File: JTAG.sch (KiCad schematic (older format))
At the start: 5 parts, among them J17 Conn_02x05_Odd_Even

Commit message: PVT
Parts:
- renumbered R89 to R79, R90 to R80, R91 to R81, RA10 to RA11
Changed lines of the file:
@@
 encoding utf-8
 Sheet 15 24
-Title "Phoenix DVT"
-Date "2020-05-18"
+Title "Phoenix PVT"
+Date "2020-07-19"
 Rev "1"
 Comp ""
@@
 P 7200 3700
 AR Path="/5E4B5786/5ED1E5C8" Ref="R?"  Part="1"
-AR Path="/5EF045E7/5ED1E5C8" Ref="R90"  Part="1"
-F 0 "R90" H 7258 3746 50  0000 L CNN
+AR Path="/5EF045E7/5ED1E5C8" Ref="R80"  Part="1"
+F 0 "R80" H 7258 3746 50  0000 L CNN
 F 1 "1k" H 7258 3655 50  0000 L CNN
 F 2 "Resistor-Chip:R_CHIP_1005_Hand_NoSilk" V 7250 3600 50  0001 C CNN
@@
 AR Path="/5E9E174E/5ED1E5DE" Ref="#PWR?"  Part="1"
 AR Path="/5E4B5786/5ED1E5DE" Ref="#PWR?"  Part="1"
-AR Path="/5EF045E7/5ED1E5DE" Ref="#PWR0287"  Part="1"
-F 0 "#PWR0287" H 5100 4450 50  0001 C CNN
+AR Path="/5EF045E7/5ED1E5DE" Ref="#PWR0275"  Part="1"
+F 0 "#PWR0275" H 5100 4450 50  0001 C CNN
 F 1 "GND" H 5100 4550 50  0000 C CNN
 F 2 "" H 5100 4700 50  0001 C CNN
@@
 P 7000 3000
 AR Path="/5E4B5786/5ED1E5F8" Ref="R?"  Part="1"
-AR Path="/5EF045E7/5ED1E5F8" Ref="R89"  Part="1"
-F 0 "R89" H 7058 3046 50  0000 L CNN
+AR Path="/5EF045E7/5ED1E5F8" Ref="R79"  Part="1"
+F 0 "R79" H 7058 3046 50  0000 L CNN
 F 1 "10k" H 7058 2955 50  0000 L CNN
 F 2 "Resistor-Chip:R_CHIP_1005_Hand_NoSilk" V 7050 2900 50  0001 C CNN
@@
 P 7400 3000
 AR Path="/5E4B5786/5ED1E601" Ref="R?"  Part="1"
-AR Path="/5EF045E7/5ED1E601" Ref="R91"  Part="1"
-F 0 "R91" H 7458 3046 50  0000 L CNN
+AR Path="/5EF045E7/5ED1E601" Ref="R81"  Part="1"
+F 0 "R81" H 7458 3046 50  0000 L CNN
 F 1 "10k" H 7458 2955 50  0000 L CNN
 F 2 "Resistor-Chip:R_CHIP_1005_Hand_NoSilk" V 7450 2900 50  0001 C CNN
@@
 AR Path="/5E4B5B3E/5ED1E618" Ref="RA?"  Part="2"
 AR Path="/5E4B5786/5ED1E618" Ref="RA?"  Part="2"
-AR Path="/5EF045E7/5ED1E618" Ref="RA10"  Part="2"
-F 0 "RA10" V 7950 3350 50  0000 R CNN
+AR Path="/5EF045E7/5ED1E618" Ref="RA11"  Part="2"
+F 0 "RA11" V 7950 3350 50  0000 R CNN
 F 1 "51" V 7950 3650 50  0000 L CNN
 F 2 "Resistor-Chip:R_CHIP_4x1005_CONCAVE" H 8000 3500 50  0001 C CNN
@@
 AR Path="/5E4B5B3E/5ED1E61E" Ref="RA?"  Part="3"
 AR Path="/5E4B5786/5ED1E61E" Ref="RA?"  Part="3"
-AR Path="/5EF045E7/5ED1E61E" Ref="RA10"  Part="3"
-F 0 "RA10" V 7950 3050 50  0000 R CNN
+AR Path="/5EF045E7/5ED1E61E" Ref="RA11"  Part="3"
+F 0 "RA11" V 7950 3050 50  0000 R CNN
 F 1 "51" V 7950 3350 50  0000 L CNN
 F 2 "Resistor-Chip:R_CHIP_4x1005_CONCAVE" H 8000 3200 50  0001 C CNN
@@
 AR Path="/5E4B5B3E/5ED1E624" Ref="RA?"  Part="4"
 AR Path="/5E4B5786/5ED1E624" Ref="RA?"  Part="4"
-AR Path="/5EF045E7/5ED1E624" Ref="RA10"  Part="4"
-F 0 "RA10" V 7950 3150 50  0000 R CNN
+AR Path="/5EF045E7/5ED1E624" Ref="RA11"  Part="4"
+F 0 "RA11" V 7950 3150 50  0000 R CNN
 F 1 "51" V 7950 3450 50  0000 L CNN
 F 2 "Resistor-Chip:R_CHIP_4x1005_CONCAVE" H 8000 3300 50  0001 C CNN
@@
 AR Path="/5E9E174E/5ED1E62A" Ref="#PWR?"  Part="1"
 AR Path="/5E4B5786/5ED1E62A" Ref="#PWR?"  Part="1"
-AR Path="/5EF045E7/5ED1E62A" Ref="#PWR0289"  Part="1"
-F 0 "#PWR0289" H 7200 3550 50  0001 C CNN
+AR Path="/5EF045E7/5ED1E62A" Ref="#PWR0277"  Part="1"
+F 0 "#PWR0277" H 7200 3550 50  0001 C CNN
 F 1 "GND" H 7200 3650 50  0000 C CNN
 F 2 "" H 7200 3800 50  0001 C CNN
@@
 AR Path="/5E4B5B3E/5ED1E636" Ref="RA?"  Part="1"
 AR Path="/5E4B5786/5ED1E636" Ref="RA?"  Part="1"
-AR Path="/5EF045E7/5ED1E636" Ref="RA10"  Part="1"
-F 0 "RA10" V 7950 3250 50  0000 R CNN
+AR Path="/5EF045E7/5ED1E636" Ref="RA11"  Part="1"
+F 0 "RA11" V 7950 3250 50  0000 R CNN
 F 1 "51" V 7950 3550 50  0000 L CNN
 F 2 "Resistor-Chip:R_CHIP_4x1005_CONCAVE" H 8000 3400 50  0001 C CNN
@@
 	7400 3400 7900 3400
 $Comp
-L supply-value:+1V8 #PWR0286
+L supply-value:+1V8 #PWR0274
 U 1 1 5F8A9579
 P 4900 4400
-F 0 "#PWR0286" H 4900 4250 50  0001 C CNN
+F 0 "#PWR0274" H 4900 4250 50  0001 C CNN
 F 1 "+1V8" H 4900 4540 50  0000 C CNN
 F 2 "" H 4900 4400 50  0001 C CNN
@@
 	7000 2800 7200 2800
 $Comp
-L supply-value:+1V8 #PWR0288
+L supply-value:+1V8 #PWR0276
 U 1 1 5F8AA51D
 P 7200 2800
-F 0 "#PWR0288" H 7200 2650 50  0001 C CNN
+F 0 "#PWR0276" H 7200 2650 50  0001 C CNN
 F 1 "+1V8" H 7200 2940 50  0000 C CNN
 F 2 "" H 7200 2800 50  0001 C CNN

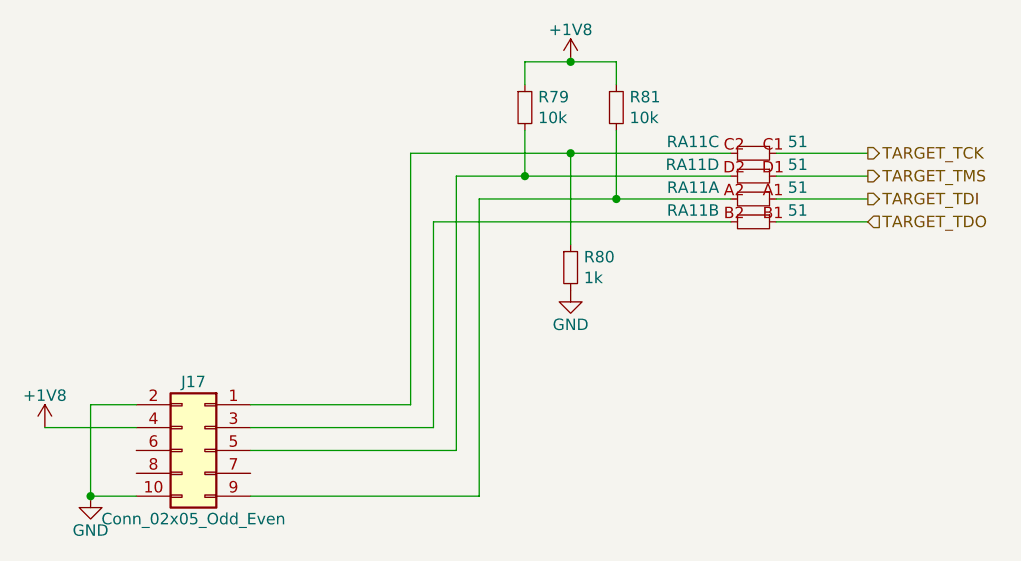
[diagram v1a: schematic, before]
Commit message: SBUにTVSダイオードを追加
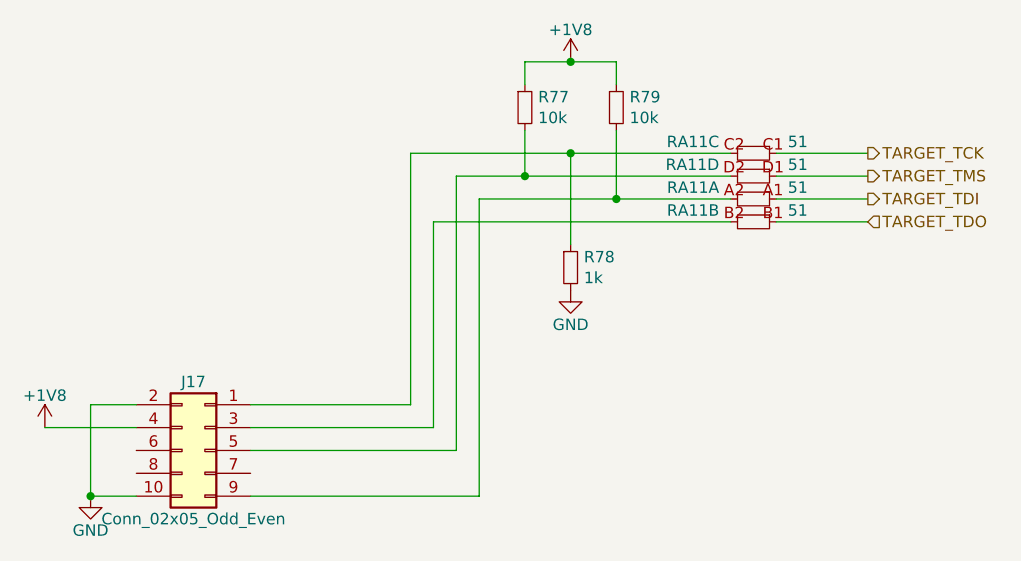
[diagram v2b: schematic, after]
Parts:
- renumbered R79 to R77, R80 to R78, R81 to R79
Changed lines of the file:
@@
 P 7200 3700
 AR Path="/5E4B5786/5ED1E5C8" Ref="R?"  Part="1"
-AR Path="/5EF045E7/5ED1E5C8" Ref="R80"  Part="1"
-F 0 "R80" H 7258 3746 50  0000 L CNN
+AR Path="/5EF045E7/5ED1E5C8" Ref="R78"  Part="1"
+F 0 "R78" H 7258 3746 50  0000 L CNN
 F 1 "1k" H 7258 3655 50  0000 L CNN
 F 2 "Resistor-Chip:R_CHIP_1005_Hand_NoSilk" V 7250 3600 50  0001 C CNN
@@
 P 7000 3000
 AR Path="/5E4B5786/5ED1E5F8" Ref="R?"  Part="1"
-AR Path="/5EF045E7/5ED1E5F8" Ref="R79"  Part="1"
-F 0 "R79" H 7058 3046 50  0000 L CNN
+AR Path="/5EF045E7/5ED1E5F8" Ref="R77"  Part="1"
+F 0 "R77" H 7058 3046 50  0000 L CNN
 F 1 "10k" H 7058 2955 50  0000 L CNN
 F 2 "Resistor-Chip:R_CHIP_1005_Hand_NoSilk" V 7050 2900 50  0001 C CNN
@@
 P 7400 3000
 AR Path="/5E4B5786/5ED1E601" Ref="R?"  Part="1"
-AR Path="/5EF045E7/5ED1E601" Ref="R81"  Part="1"
-F 0 "R81" H 7458 3046 50  0000 L CNN
+AR Path="/5EF045E7/5ED1E601" Ref="R79"  Part="1"
+F 0 "R79" H 7458 3046 50  0000 L CNN
 F 1 "10k" H 7458 2955 50  0000 L CNN
 F 2 "Resistor-Chip:R_CHIP_1005_Hand_NoSilk" V 7450 2900 50  0001 C CNN
